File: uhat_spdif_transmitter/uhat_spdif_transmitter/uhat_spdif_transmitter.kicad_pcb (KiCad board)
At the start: 2 copper layers, 65 x 30 mm, 75 parts, among them J1 GPIO_CONNECTOR, Q1 SS8050, SW1 SW_Push, U1 PLT131/T8, U10 USBLC6-2SC6, U2 LR8103A-T12, U4 W25Q32JVSSIQ, U5 24LC256T-I/SN, U6 PLT131/T8, U8 ICE40UP5K-SG48I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

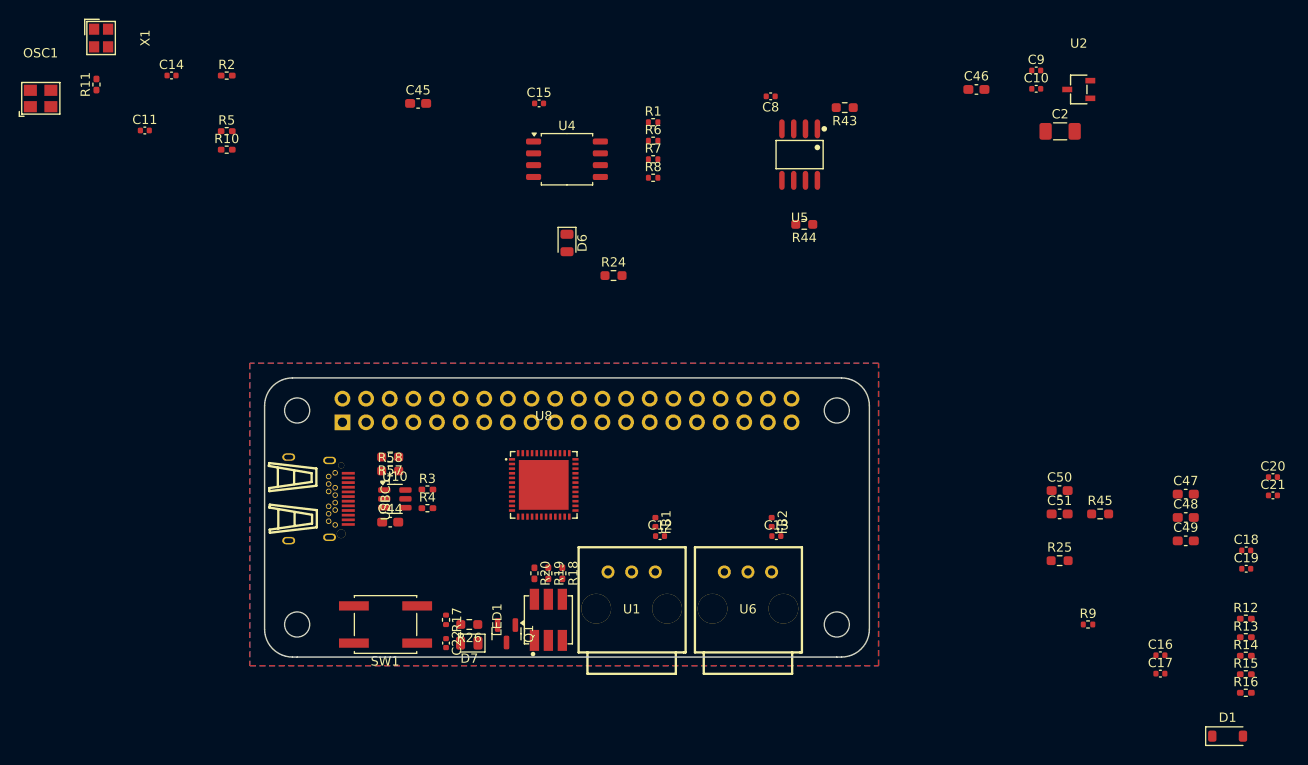
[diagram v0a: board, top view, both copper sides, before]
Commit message: update 3d models, component placement
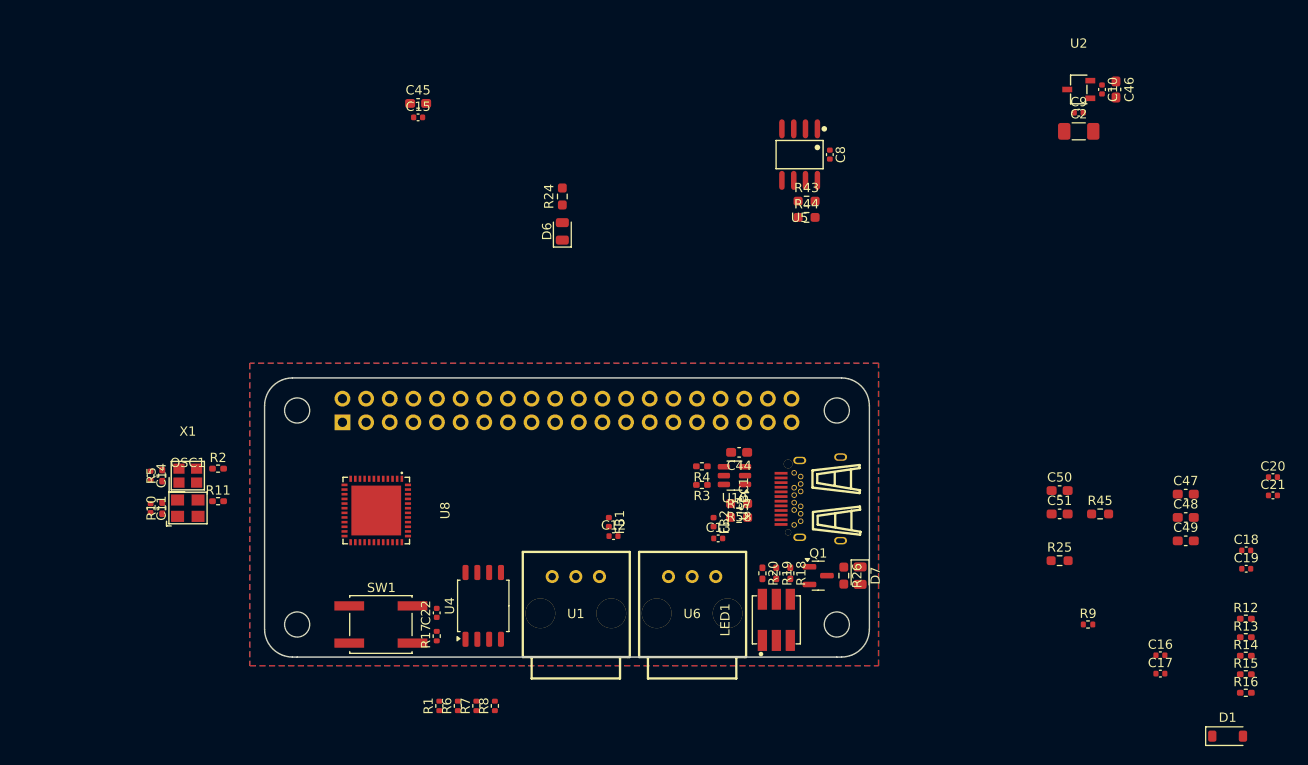
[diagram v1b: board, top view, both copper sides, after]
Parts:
- moved R1 66.8 mm to (136.3, 126.3), turned to 90 degrees
- moved R6 64.3 mm to (138.3, 126.3), turned to 90 degrees
- moved R7 61.7 mm to (140.3, 126.3), turned to 90 degrees
- moved R8 59.3 mm to (142.3, 126.3), turned to 90 degrees
- moved USBC1 52.9 mm to (176.2, 104.1), turned to 90 degrees
- moved U4 48.8 mm to (141.0, 115.6), turned to 90 degrees
- moved X1 47.9 mm to (109.3, 101.6), turned to 0 degrees
- moved OSC1 46.8 mm to (109.3, 105.1)
- moved R11 46.6 mm to (112.5, 104.3), turned to 0 degrees
- moved C14 43.1 mm to (105.3, 101.6), turned to -90 degrees
- moved D7 42.6 mm to (181.5, 112.3), turned to -90 degrees
- moved R2 42.3 mm to (112.5, 100.8)
- moved C11 40.6 mm to (105.3, 105.1), turned to -90 degrees
- moved R26 40.6 mm to (179.8, 112.3), turned to -90 degrees
- moved R10 39.1 mm to (106.5, 105.1), turned to 90 degrees
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
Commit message: layout
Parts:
- added J2: Conn_02x03_Odd_Even, Connector_PinHeader_2.54mm:PinHeader_2x03_P2.54mm_Vertical_SMD, F.Cu at (151.5, 103.3)
- added J3: Conn_01x03_Pin, Connector_PinHeader_2.54mm:PinHeader_1x03_P2.54mm_Vertical_SMD_Pin1Left, F.Cu at (159.6, 104.1)
- added REF**: Raspberry Pi Zero 2 W, Locrius_KiCad:Raspberry Pi Zero 2 W, F.Cu at (149.8, 106.1)
- R25, R43, R44: footprint Resistor_SMD:R_0603_1608Metric_Pad0.98x0.95mm_HandSolder -> Resistor_SMD:R_0402_1005Metric
- R3, R4: value 27R -> 68R
- SW1: value SW_Push -> SPEH110100; footprint Button_Switch_SMD:SW_SPST_EVQQ2 -> Locrius_KiCad:SW-SMD_L6.0-W6.0-LS6.6
- moved D1 101.9 mm to (122.0, 105.6), turned to 180 degrees
- moved R16 95.1 mm to (129.0, 110.3), turned to -90 degrees
- moved R15 93.8 mm to (130.0, 110.3), turned to -90 degrees
- moved C20 90.4 mm to (135.8, 109.1)
- moved C19 89.7 mm to (134.3, 98.6), turned to 90 degrees
- moved C21 89.5 mm to (136.5, 98.8), turned to 90 degrees
- moved C18 88.8 mm to (134.3, 110.1), turned to 90 degrees
- moved C16 88.1 mm to (127.0, 105.8), turned to 90 degrees
- moved R14 84.8 mm to (140.3, 102.3)
- moved R12 84.2 mm to (140.3, 101.3)
- moved R13 84.2 mm to (140.3, 103.3)
- moved C46 82.7 mm to (140.8, 106.8), turned to 90 degrees
- moved C17 82.7 mm to (132.3, 109.1), turned to 180 degrees
- moved C47 81.7 mm to (135.3, 111.8)
- moved C10 80.3 mm to (142.3, 106.8), turned to 90 degrees
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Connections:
- net /DM renamed /DN
- R12 pad 2: /PCM_FCLK -> /FPGA_FCLK
- R13 pad 2: /PCM_BCLK -> /FPGA_BCLK
- R14 pad 2: /PCM_DOUT -> /FPGA_DOUT
- U8 pad 10: /QSPI_SD2 -> unconnected-(U8-IOB_18a-Pad10)
- U8 pad 14: /QSPI_SD0 -> /SPI_MOSI
- U8 pad 15: /QSPI_SCLK -> /SPI_SCK
- U8 pad 16: /QSPI_SS -> /SPI_SS
- U8 pad 17: /QSPI_SD1 -> /SPI_MISO
- U8 pad 20: /QSPI_SD3 -> unconnected-(U8-IOB_25b_G3-Pad20)
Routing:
- net /USER_LED: track 0.00 -> 55.3 mm, vias 0 -> 2
- net /DP: track 0.00 -> 47.2 mm, vias 0 -> 2
- net +3V3: track 0.00 -> 42.2 mm, vias 0 -> 15
- net /DN: track 0.00 -> 40.6 mm, vias 0 -> 2
- net /RGB1: track 0.00 -> 40.3 mm, vias 0 -> 2
- net /RGB2: track 0.00 -> 39.0 mm, vias 0 -> 2
- net /PCM_DOUT: track 0.00 -> 38.4 mm, vias 0 -> 1
- net /RGB0: track 0.00 -> 37.1 mm, vias 0 -> 2
- net /PCM_FCLK: track 0.00 -> 31.0 mm, vias 0 -> 1
- net /UART_TX: track 0.00 -> 24.8 mm, vias 0 -> 1
- net /UART_RX: track 0.00 -> 23.8 mm, vias 0 -> 1
- net Net-(U10-VBUS): track 0.00 -> 21.5 mm, vias 0 -> 4
- net /CRESET: track 0.00 -> 18.2 mm, vias 0 -> 1
- net Net-(USBC1-CC2): track 0.00 -> 18.1 mm, vias 0 -> 1
- net /D-: track 0.00 -> 14.8 mm, vias 0 -> 1
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- added copper zone on In1.Cu, net +1V2
- added copper zone on In1.Cu, net +3V3
- added copper zone on In2.Cu, net GND
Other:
- copper layers 2 -> 4

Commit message: Finish routing
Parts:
- removed D7: C2290, LED_SMD:LED_0805_2012Metric
- removed LED1: TC5050RGBF08-3CJH-AF53A, Locrius_KiCad:LED-SMD_6P-L5.0-W5.0-TL_TC5050RGBF08
- removed Q1: SS8050, Package_TO_SOT_SMD:SOT-23
- removed R26: 2k2, Resistor_SMD:R_0603_1608Metric_Pad0.98x0.95mm_HandSolder
- removed REF**: Raspberry Pi Zero 2 W, Locrius_KiCad:Raspberry Pi Zero 2 W
- removed SW1: SPEH110100, Locrius_KiCad:SW-SMD_L6.0-W6.0-LS6.6
- added J4: Conn_02x03_Odd_Even, Connector_PinHeader_2.54mm:PinHeader_2x03_P2.54mm_Vertical, F.Cu at (119.7, 100.0)
- added LED2: MHS110RGBCT, Locrius_KiCad:LED-ARRAY-SMD_MHS110RGBCT, F.Cu at (144.0, 120.3)
- added SW2: SKRTLAE010, Locrius_KiCad:KEY-SMD_SKRTLAE010, F.Cu at (127.3, 119.6)
- J2: footprint Connector_PinHeader_2.54mm:PinHeader_2x03_P2.54mm_Vertical_SMD -> Connector_PinHeader_2.54mm:PinHeader_2x03_P2.54mm_Vertical
- J3: footprint Connector_PinHeader_2.54mm:PinHeader_1x03_P2.54mm_Vertical_SMD_Pin1Left -> Connector_PinHeader_2.54mm:PinHeader_1x03_P2.54mm_Vertical
- R25, R43, R44: footprint Resistor_SMD:R_0402_1005Metric -> Resistor_SMD:R_0603_1608Metric_Pad0.98x0.95mm_HandSolder
- U1, U6: value PLT131/T8 -> PLR237/T10BK; footprint Locrius_KiCad:OPTO-TH_PLT131-T8 -> Locrius_KiCad:OPTO-TH_PLR237-T10BK
- moved U5 38.4 mm to (159.8, 106.3), turned to 90 degrees
- moved C8 38.0 mm to (159.8, 103.1), turned to 180 degrees
- moved R43 37.0 mm to (161.4, 111.0), turned to -90 degrees
- moved R18 31.0 mm to (143.5, 117.6)
- moved R44 29.4 mm to (157.0, 101.6)
- moved R19 27.5 mm to (145.5, 117.6)
- moved R20 27.1 mm to (144.5, 117.6)
- moved C22 9.76 mm to (126.3, 116.8), turned to 180 degrees
- moved C2 9.76 mm to (145.3, 111.1)
- moved J3 8.75 mm to (152.3, 99.3), turned to 0 degrees
- moved C12 8.50 mm to (154.3, 109.1)
- moved FB1 8.50 mm to (152.0, 109.1)
- moved R6 7.87 mm to (141.2, 118.2), turned to 180 degrees
- moved R17 7.76 mm to (128.5, 116.8), turned to 180 degrees
- moved C9 7.40 mm to (143.3, 111.6), turned to 90 degrees
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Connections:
- U1 pad 1: GND -> Net-(U1-VCC)
- U1 pad 2: /OPT1 -> GND
- U1 pad 3: Net-(U1-VCC) -> /OPT1
- U6 pad 1: GND -> Net-(U6-VCC)
- U6 pad 2: /OPT2 -> GND
- U6 pad 3: Net-(U6-VCC) -> /OPT2
- U8 pad 10: unconnected-(U8-IOB_18a-Pad10) -> Net-(J4-Pin_4)
- U8 pad 11: unconnected-(U8-IOB_20a-Pad11) -> Net-(J4-Pin_6)
- U8 pad 19: /USER_LED -> unconnected-(U8-IOB_29b-Pad19)
- U8 pad 9: unconnected-(U8-IOB_16a-Pad9) -> Net-(J4-Pin_2)
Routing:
- net /SPI_SS: track 5.31 -> 81.3 mm, vias 2 -> 4
- net /SPI_MISO: track 3.38 -> 77.7 mm, vias 2 -> 4
- net /SPI_MOSI: track 3.04 -> 71.4 mm, vias 2 -> 4
- net /SPI_SCK: track 4.51 -> 70.7 mm, vias 2 -> 3
- net /USER_LED: track 55.3 -> 0.00 mm, vias 2 -> 0
- net /OPT2: track 0.90 -> 51.9 mm
- net /OPT1: track 0.90 -> 37.0 mm
- net /CDONE: track 0.00 -> 35.0 mm, vias 0 -> 1
- net /ID_SC: track 0.00 -> 27.4 mm
- net /RGB1: track 40.3 -> 15.6 mm
- net /RGB2: track 39.0 -> 17.5 mm
- net /RGB0: track 37.1 -> 15.6 mm
- net /USER_SW: track 5.98 -> 26.3 mm
- net Net-(J4-Pin_6): track 0.00 -> 12.7 mm
- net Net-(J4-Pin_2): track 0.00 -> 12.3 mm
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
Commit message: Finish layouting
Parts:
- added REF**: Raspberry Pi Zero 2 W, Locrius_KiCad:Raspberry Pi Zero 2 W, F.Cu at (150.0, 106.1)
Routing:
- net GND: vias 12 -> 44
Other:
- board text added: "B"
- board text added: "BCK"
- board text added: "CDONE"
- board text added: "D"
- board text added: "DAT"
- board text added: "F"
- board text added: "FCK"
- board text added: "FPGA PROG"
- board text added: "GND"
- board text added: "MPS Axign 00A - NtB"
- board text added: "OPT1"
- board text added: "OPT2"

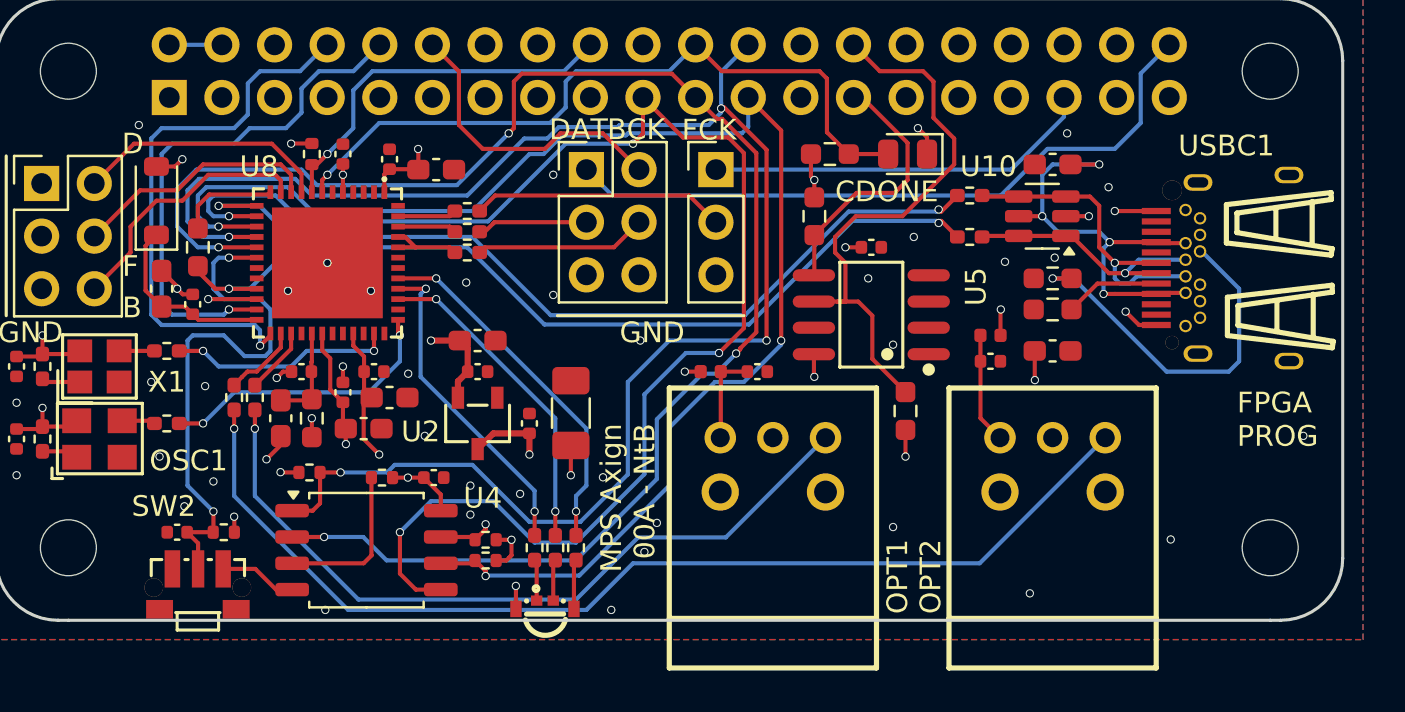
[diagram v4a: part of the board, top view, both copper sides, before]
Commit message: Change push button, add barcode location
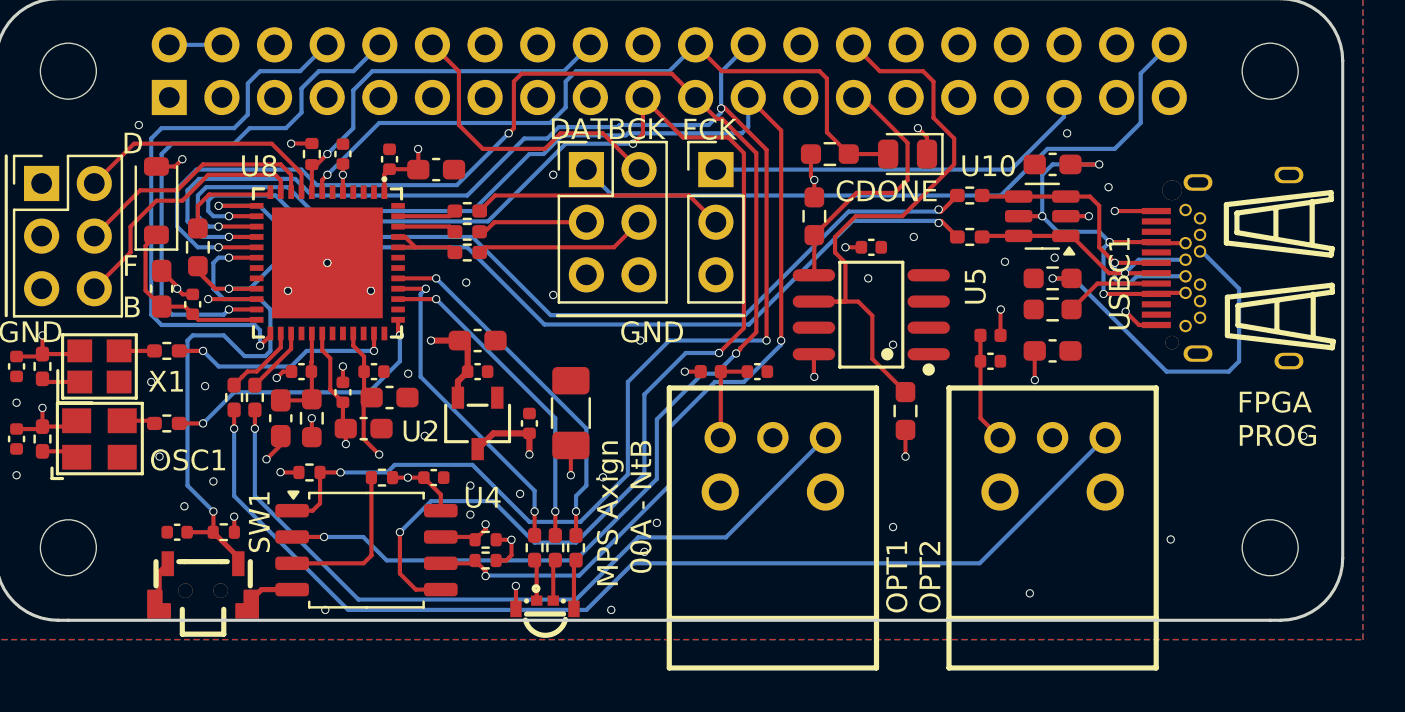
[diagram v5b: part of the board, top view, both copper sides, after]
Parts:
- removed SW2: SKRTLAE010, Locrius_KiCad:KEY-SMD_SKRTLAE010
- added SW1: TS24CA, Locrius_KiCad:SW-SMD_TS24CA, F.Cu at (127.5, 119.3)
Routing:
- net GND: track 14.6 -> 16.2 mm
